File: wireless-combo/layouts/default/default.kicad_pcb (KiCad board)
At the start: 4 copper layers, 50 x 40 mm, 34 parts

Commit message: wireless-combo: 版数をプロジェクト変数 BOARD_REV に移す
atopile 0.15.9 の PCB パーサは title_block の (rev ...) を "revision" として
読むため取りこぼし、ato build のたびに rev が消えてシルクの ${REVISION} が
空になる。版数は atopile が触らない .kicad_pro のテキスト変数 BOARD_REV に
置き、シルクと Fabrication Toolkit の ARCHIVE_NAME はそれを参照する
(ARCHIVE_NAME はプラグインが ExpandTextVars でプロジェクト変数まで展開する)。
title_block の rev は図面枠用に残すが、正は BOARD_REV。

3 基板とも ato build 後に BOARD_REV と ${BOARD_REV} 参照が残り、
シルクが v1.0.0 と描画されることを作業コピーで確認済み。

Co-Authored-By: Claude Opus 5.5 <noreply@anthropic.com>
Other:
- board text added: "${BOARD_REV} Developed by @kunichiko"
- board text removed: "${REVISION} Developed by @kunichiko"
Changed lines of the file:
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@@
 		)
 	)
-	(gr_text "${REVISION} Developed by @kunichiko"
+	(gr_text "${BOARD_REV} Developed by @kunichiko"
 		(at 117.75 85.5 270)
 		(layer "F.SilkS")

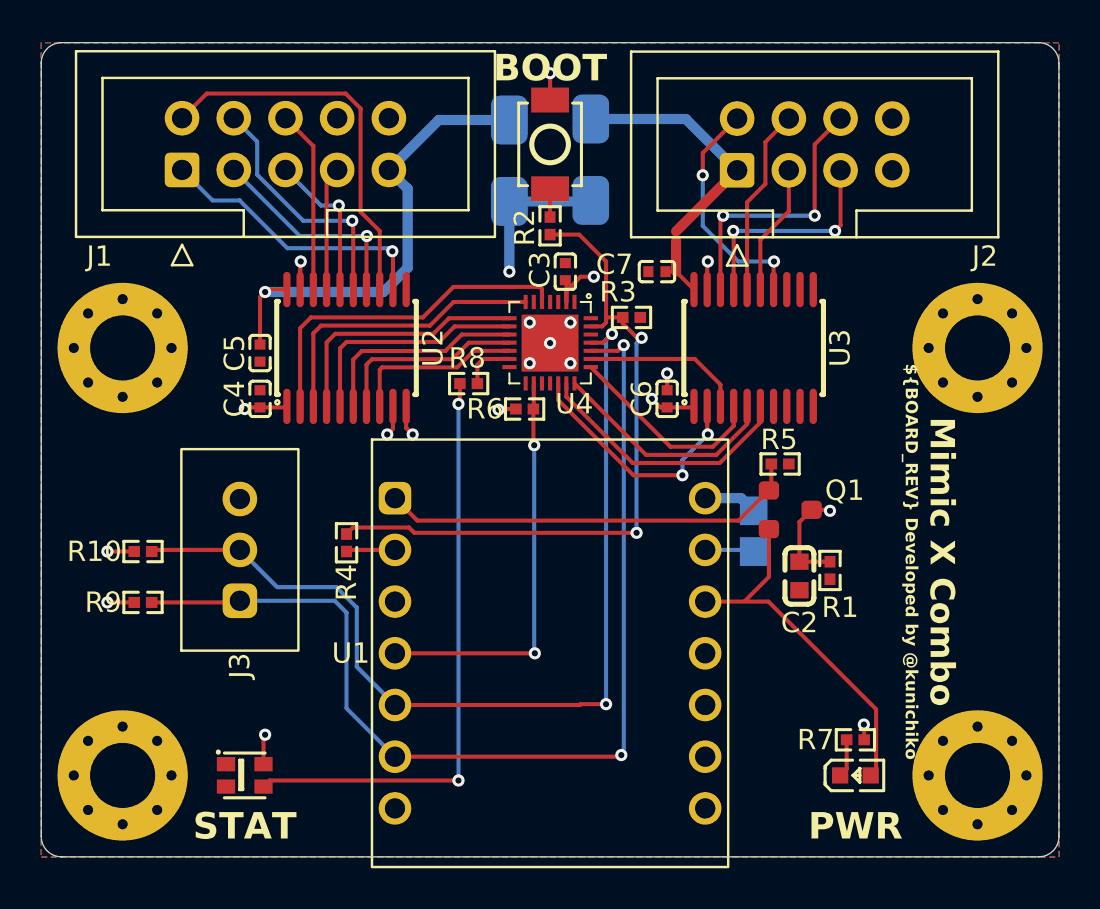
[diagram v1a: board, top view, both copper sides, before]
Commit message: wireless-combo: D1/D2 を B5819W (SOD-123) に、J3 を未実装に、変換基板を -bo 名に改名
- D1/D2: SS14 (SMA) → B5819W SL (SOD-123, LCSC C8598)。小さくなったので表面へ移動。
  フットプリントは KiCad 標準 Diode_SMD:D_SOD-123 のコピー (NOTICE に追記)
- J3 (SWD デバッグ端子 XH 3P) を BOM / CPL から除外。必要時のみ手はんだ
- default の v1.0.0 製造データを再生成
- 変換基板のビルド名 / レイアウト / エントリを改名 (将来の他機種用を見越して対象機名を付与):
  joystick → atari-joystick-bo (atari_joystick_bo.ato:AtariJoystickBo)
  keyboard → x68000-keyboard-bo (x68000_keyboard_bo.ato:X68000KeyboardBo)

Co-Authored-By: Claude Opus 5.5 <noreply@anthropic.com>
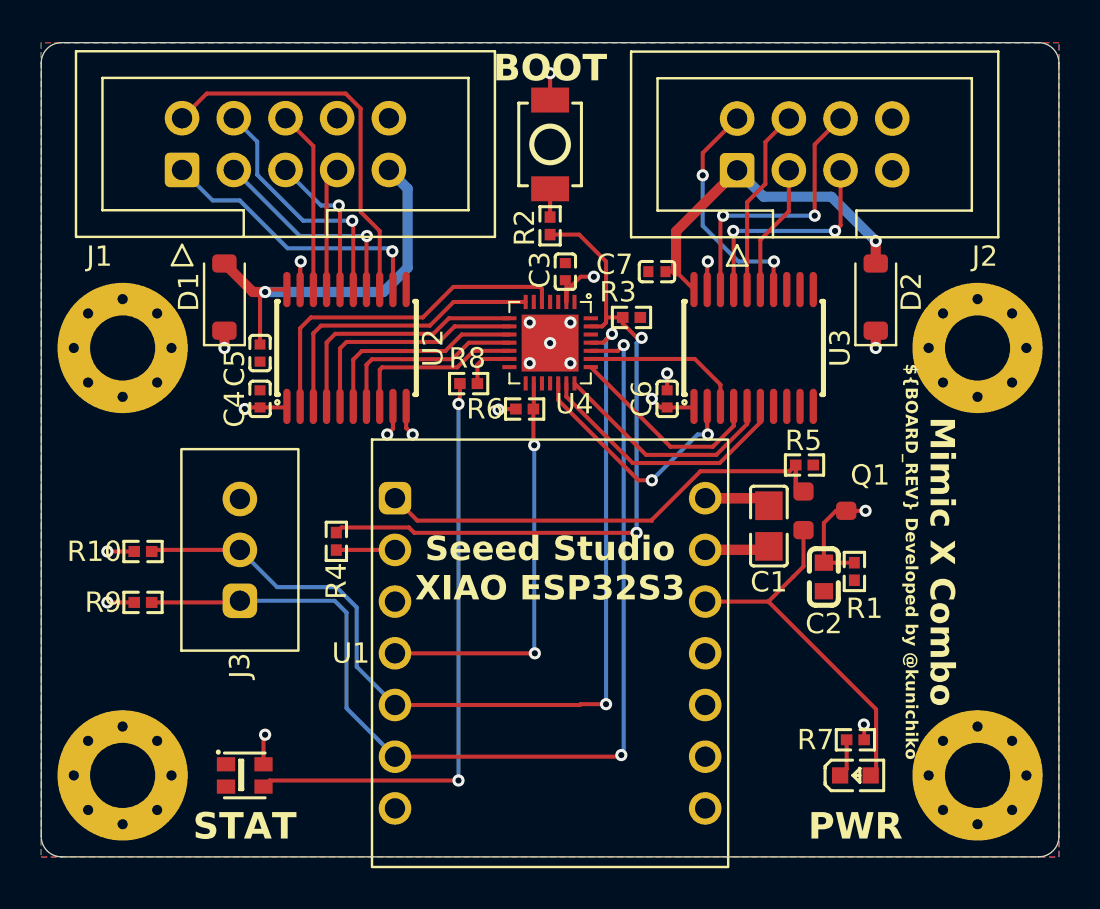
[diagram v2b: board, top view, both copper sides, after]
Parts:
- C1: moved to F.Cu
- D1, D2: footprint SS14_SMA:SS14_SMA -> B5819W_SOD123:B5819W_SOD123; moved to F.Cu
- moved D2 15.5 mm to (116.0, 72.5)
- moved D1 15.5 mm to (84.0, 72.5)
- moved Q1 1.70 mm to (113.5, 83.0)
- moved C2 1.20 mm to (113.5, 86.2)
- moved R1 1.20 mm to (115.0, 86.0)
- moved R5 1.20 mm to (112.5, 80.8)
- moved C1 0.79 mm to (110.8, 83.8)
- moved R4 0.50 mm to (89.5, 84.5)
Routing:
- net VCC_ESP: track 28.0 -> 45.4 mm, vias 1 -> 2
- net VCC_JOY: track 24.2 -> 19.8 mm
- net GND: track 10.8 -> 14.1 mm
- net CH32_PWR_OFF: track 20.8 -> 23.9 mm
- net VCC_KBD: track 16.2 -> 17.8 mm, vias 0 -> 1
- net VDD_SW: track 19.2 -> 20.1 mm
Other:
- board text added: "Seeed Studio XIAO ESP32S3"

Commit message: フルカラー LED を WS2812B-2020-V6 (C52917434) に置き換え
x68000-keyboard / atari-joystick-slim / wireless-combo のステータス LED を
旧品 WS2812B-2020 (C965555, 電源 3.5V〜) から同外形・同ピン配置の
WS2812B-2020-V6 (電源 3.3〜5.3V) に置き換え、3.3V 給電を定格内にする。

- parts/Worldsemi_WS2812B_2020_V6 を追加 (3D モデルは旧品のものを流用)、旧部品を削除
- パッド位置はほぼ同一のため配線は不変、ゾーンのみ再充填 (DRC 0/0)
- x68000-keyboard v1.0.1 / combo v1.0.0 の製造データを再生成
- atari-joystick (rev 1.0.0 製造済み) は変更しない

Co-Authored-By: Claude Opus 5.5 <noreply@anthropic.com>
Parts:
- LED2: footprint Worldsemi_WS2812B_2020:LED-SMD_4P-L2.0-W2.0-TL_WS2812B-2020 -> Worldsemi_WS2812B_2020_V6:LED-SMD_4P-L2.2-W2.0-P1.00_WS2815C-2020-4P
